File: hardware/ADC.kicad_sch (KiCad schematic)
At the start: 4 parts, among them U2 ADS114S08BIPBSR

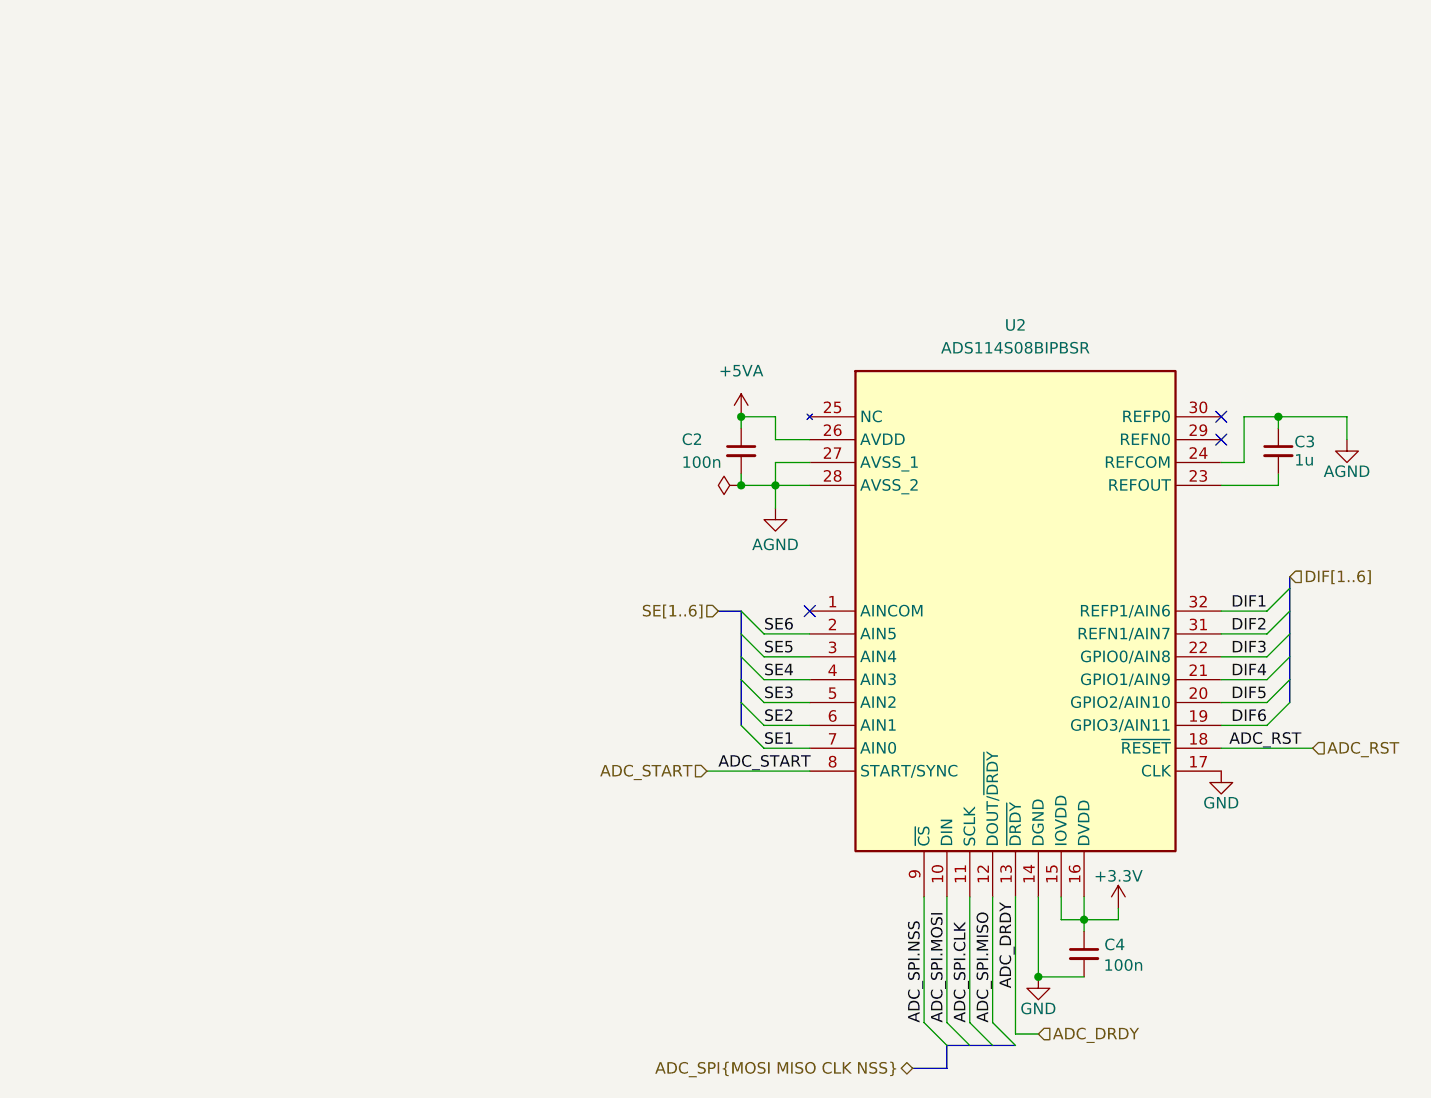
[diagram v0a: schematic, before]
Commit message: Finished routing on PCB
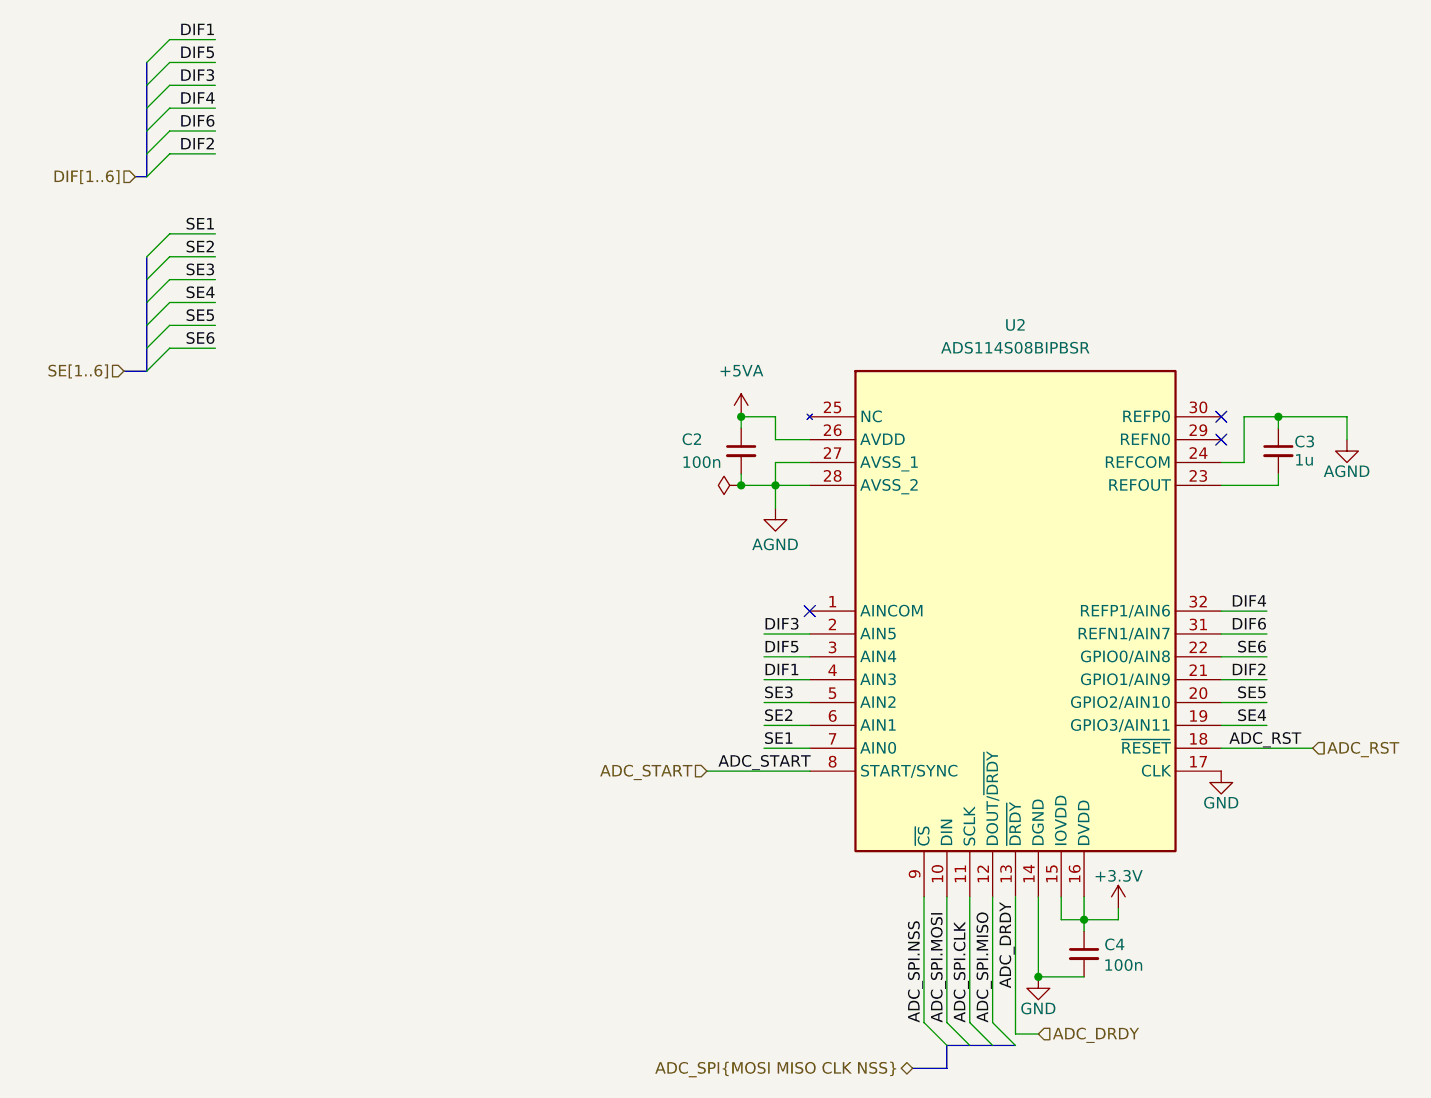
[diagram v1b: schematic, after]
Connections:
- net DIF1: now also U2.4 (AIN3); no longer U2.32 (REFP1/AIN6)
- net DIF2: now also U2.21 (GPIO1/AIN9); no longer U2.31 (REFN1/AIN7)
- net DIF3: now also U2.2 (AIN5); no longer U2.22 (GPIO0/AIN8)
- net DIF4: now also U2.32 (REFP1/AIN6); no longer U2.21 (GPIO1/AIN9)
- net DIF5: now also U2.3 (AIN4); no longer U2.20 (GPIO2/AIN10)
- net DIF6: now also U2.31 (REFN1/AIN7); no longer U2.19 (GPIO3/AIN11)
- net SE4: now also U2.19 (GPIO3/AIN11); no longer U2.4 (AIN3)
- net SE5: now also U2.20 (GPIO2/AIN10); no longer U2.3 (AIN4)
- net SE6: now also U2.22 (GPIO0/AIN8); no longer U2.2 (AIN5)

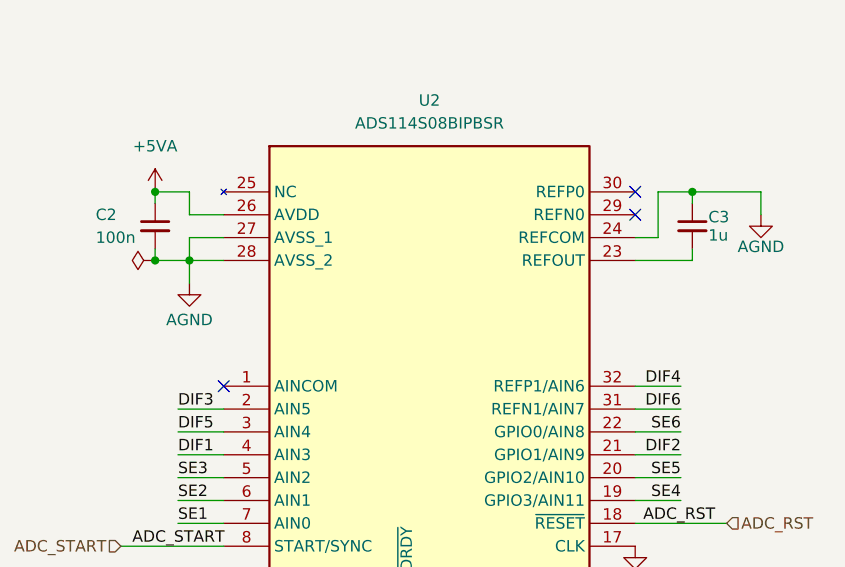
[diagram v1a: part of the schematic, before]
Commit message: Corrections after review
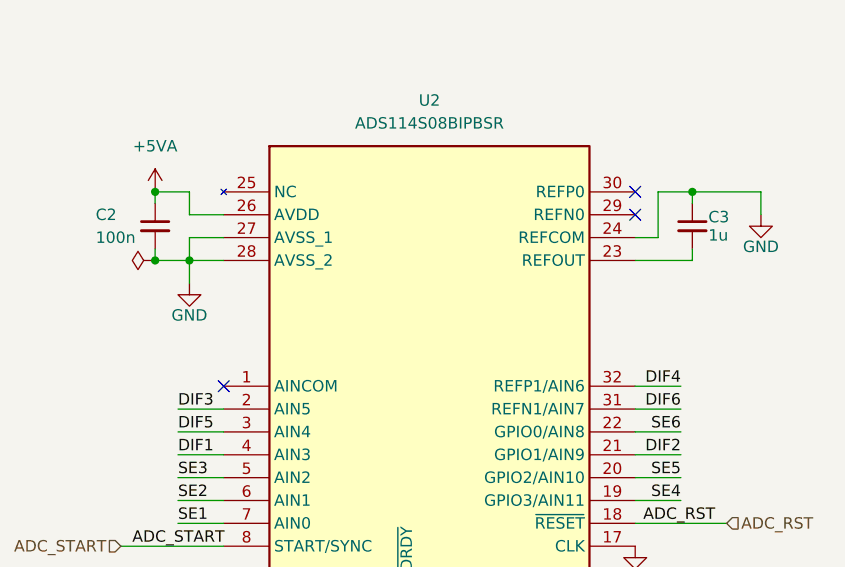
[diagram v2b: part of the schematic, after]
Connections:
- net AGND is gone; now on net GND: C2.2, C3.1, U2.24 (REFCOM), U2.27 (AVSS_1), U2.28 (AVSS_2)
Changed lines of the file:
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@@
 			)
 		)
-		(property "Value" "AGND"
+		(property "Value" "GND"
 			(at 185.42 77.216 0)
 			(effects
@@
 	)
 	(symbol
-		(lib_id "power:GND")
-		(at 121.92 81.28 0)
-		(mirror y)
-		(unit 1)
-		(exclude_from_sim no)
-		(in_bom yes)
-		(on_board yes)
-		(dnp no)
-		(property "Reference" "#PWR06"
-			(at 121.92 87.63 0)
-			(effects
-				(font
-					(size 1.27 1.27)
-				)
-				(hide yes)
-			)
-		)
-		(property "Value" "AGND"
-			(at 121.92 85.344 0)
-			(effects
-				(font
-					(size 1.27 1.27)
-				)
-			)
-		)
-		(property "Footprint" ""
-			(at 121.92 81.28 0)
-			(effects
-				(font
-					(size 1.27 1.27)
-				)
-				(hide yes)
-			)
-		)
-		(property "Datasheet" ""
-			(at 121.92 81.28 0)
-			(effects
-				(font
-					(size 1.27 1.27)
-				)
-				(hide yes)
-			)
-		)
-		(property "Description" "Power symbol creates a global label with name \"GND\" , ground"
-			(at 121.92 81.28 0)
-			(effects
-				(font
-					(size 1.27 1.27)
-				)
-				(hide yes)
-			)
-		)
-		(pin "1"
-		)
-		(instances
-			(project "UMB"
-				(path "/b652b05a-4e3d-4ad1-b032-18886abe7d45/27728c5b-995e-4e9b-804c-adae9f98b692"
-					(reference "#PWR06")
-					(unit 1)
-				)
-			)
-		)
-	)
-	(symbol
 		(lib_name "ADS114S08BIPBSR_1")
 		(lib_id "ADS114S08BIPBSR:ADS114S08BIPBSR")
@@
 					(unit 1)
 				)
+			)
+		)
+	)
+	(symbol
+		(lib_id "power:GND")
+		(at 121.92 81.28 0)
+		(unit 1)
+		(exclude_from_sim no)
+		(in_bom yes)
+		(on_board yes)
+		(dnp no)
+		(property "Reference" "#PWR048"
+			(at 121.92 87.63 0)
+			(effects
+				(font
+					(size 1.27 1.27)
+				)
+				(hide yes)
+			)
+		)
+		(property "Value" "GND"
+			(at 121.92 84.836 0)
+			(effects
+				(font
+					(size 1.27 1.27)
+				)
+			)
+		)
+		(property "Footprint" ""
+			(at 121.92 81.28 0)
+			(effects
+				(font
+					(size 1.27 1.27)
+				)
+				(hide yes)
+			)
+		)
+		(property "Datasheet" ""
+			(at 121.92 81.28 0)
+			(effects
+				(font
+					(size 1.27 1.27)
+				)
+				(hide yes)
+			)
+		)
+		(property "Description" "Power symbol creates a global label with name \"GND\" , ground"
+			(at 121.92 81.28 0)
+			(effects
+				(font
+					(size 1.27 1.27)
+				)
+				(hide yes)
+			)
+		)
+		(pin "1"
+		)
+		(instances
+			(project "UMB"
+				(path "/b652b05a-4e3d-4ad1-b032-18886abe7d45/27728c5b-995e-4e9b-804c-adae9f98b692"
+					(reference "#PWR048")
+					(unit 1)
+				)

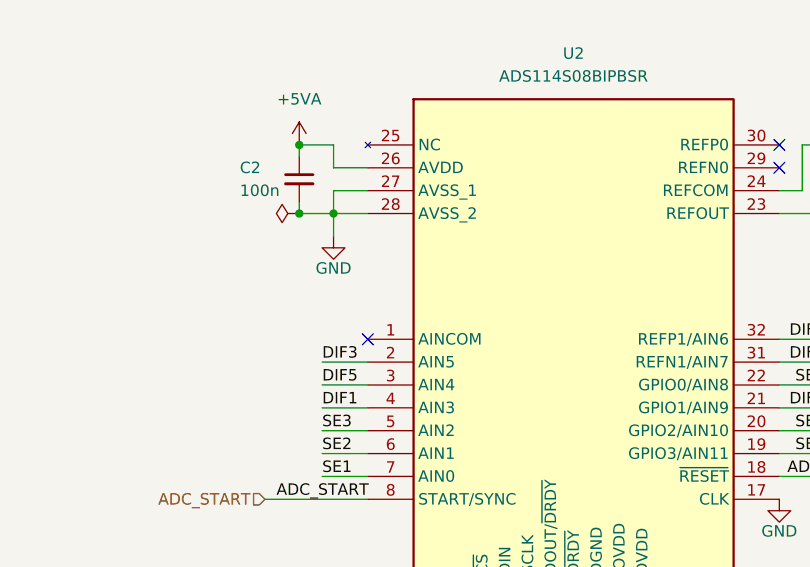
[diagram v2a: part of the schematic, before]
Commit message: Fixed pinout errors & changed branch name
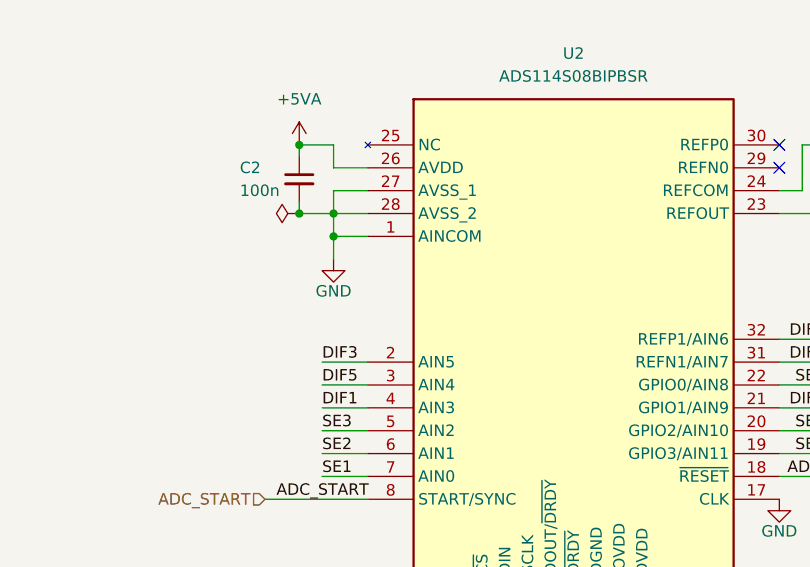
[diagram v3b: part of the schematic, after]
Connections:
- net GND: now also U2.1 (AINCOM)
- no-connect marks 3 -> 2

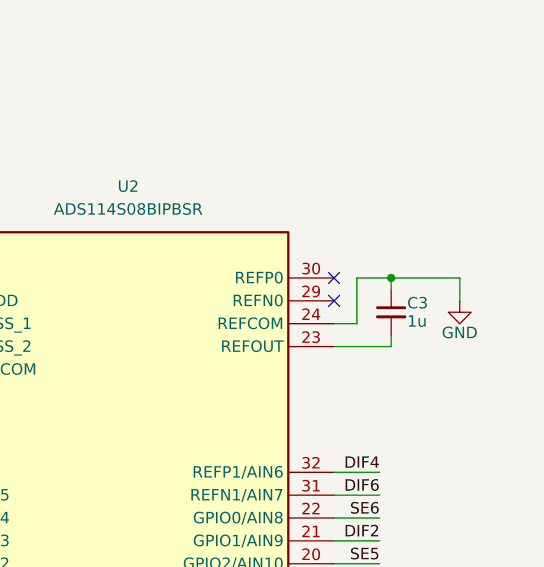
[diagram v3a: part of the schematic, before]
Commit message: ADC Ref pins connection fix
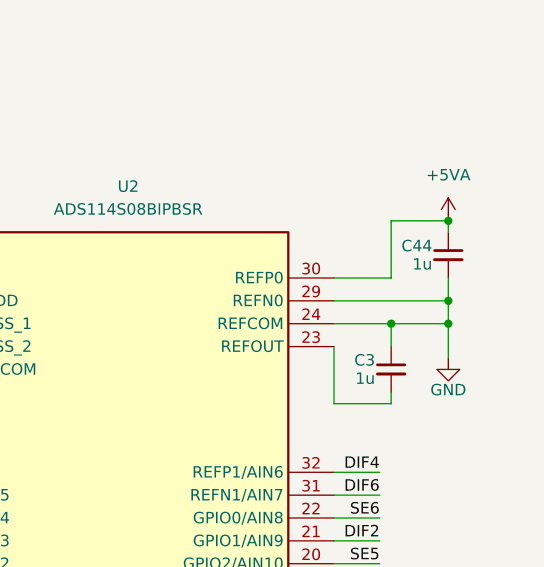
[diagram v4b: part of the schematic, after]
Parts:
- added C44: 1u, Capacitor_SMD:C_0603_1608Metric_Pad1.08x0.95mm_HandSolder, symbol Device:C_Small
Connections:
- net +5VA: now also U2.30 (REFP0), C44.1
- net GND: now also U2.29 (REFN0), C44.2
- no-connect marks 2 -> 0
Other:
- moved on the sheet: C3
